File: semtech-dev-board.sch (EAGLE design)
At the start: 58 parts, among them Q1 BSS123, Q2 32MHz, U1 SEMTECH_SX1236, U3 MIC5219 3.3V, X1 BU-SMA-G, X2 BU-SMA-G, X3 BU-SMA-G, X4 BU-SMA-G

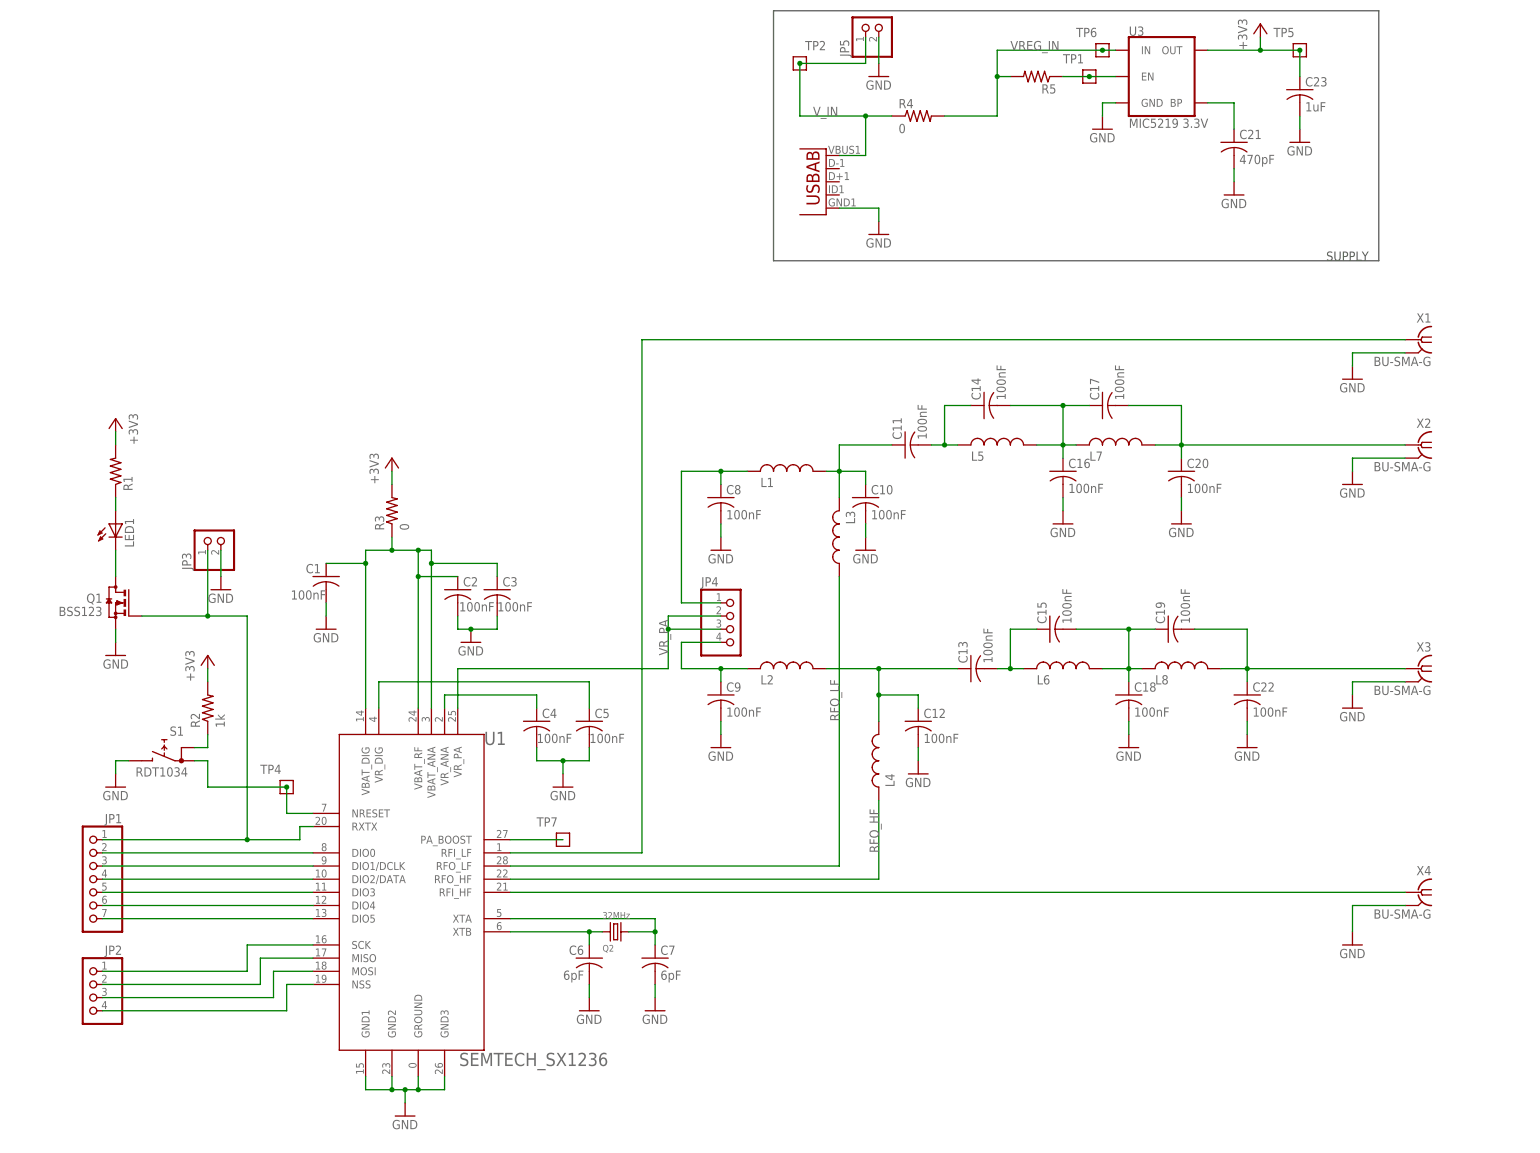
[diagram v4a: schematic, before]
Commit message: Removed caps
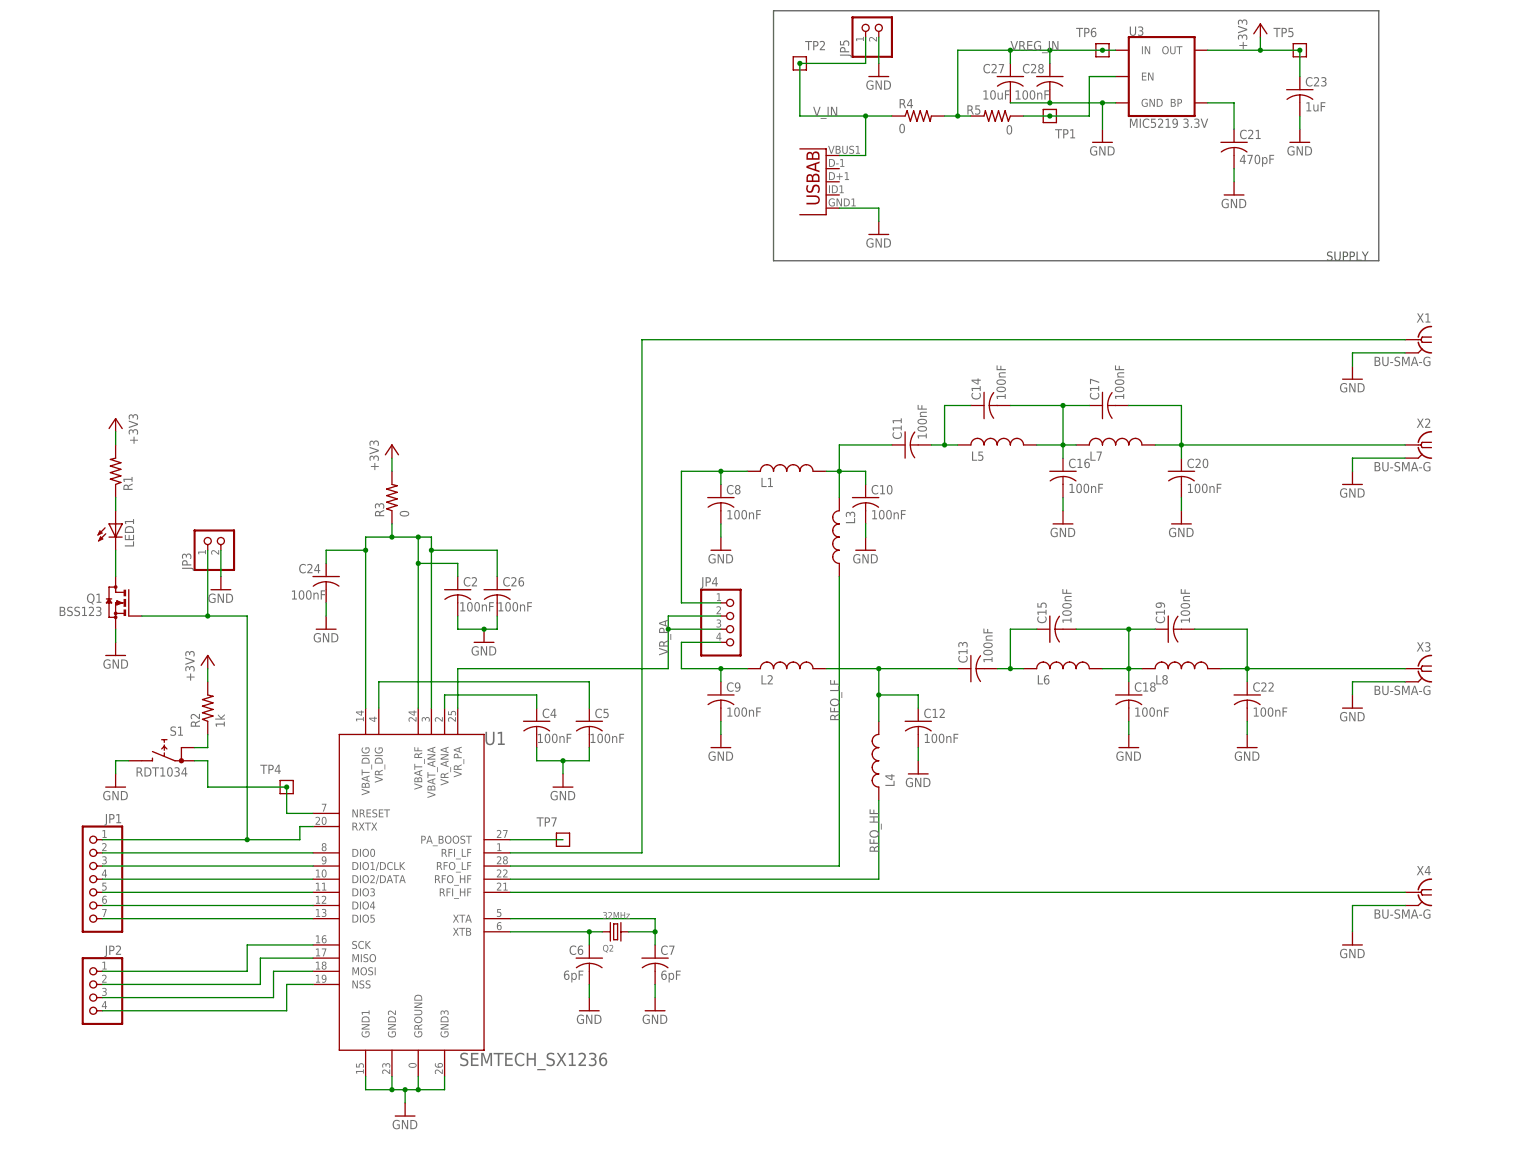
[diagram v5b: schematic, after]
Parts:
- added C27: 10uF, rcl:C-USC0805
- added C28: 100nF, rcl:C-USC0805
- R5: value (none) -> 0
- renumbered C1 to C24, C3 to C26
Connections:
- net 5219_EN renamed N$1
- net GND: now also C27.2, C28.2
- net VREG_IN: now also C27.1, C28.1
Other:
- moved on the sheet: R3, R5, TP1

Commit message: Components placed, 80% routed
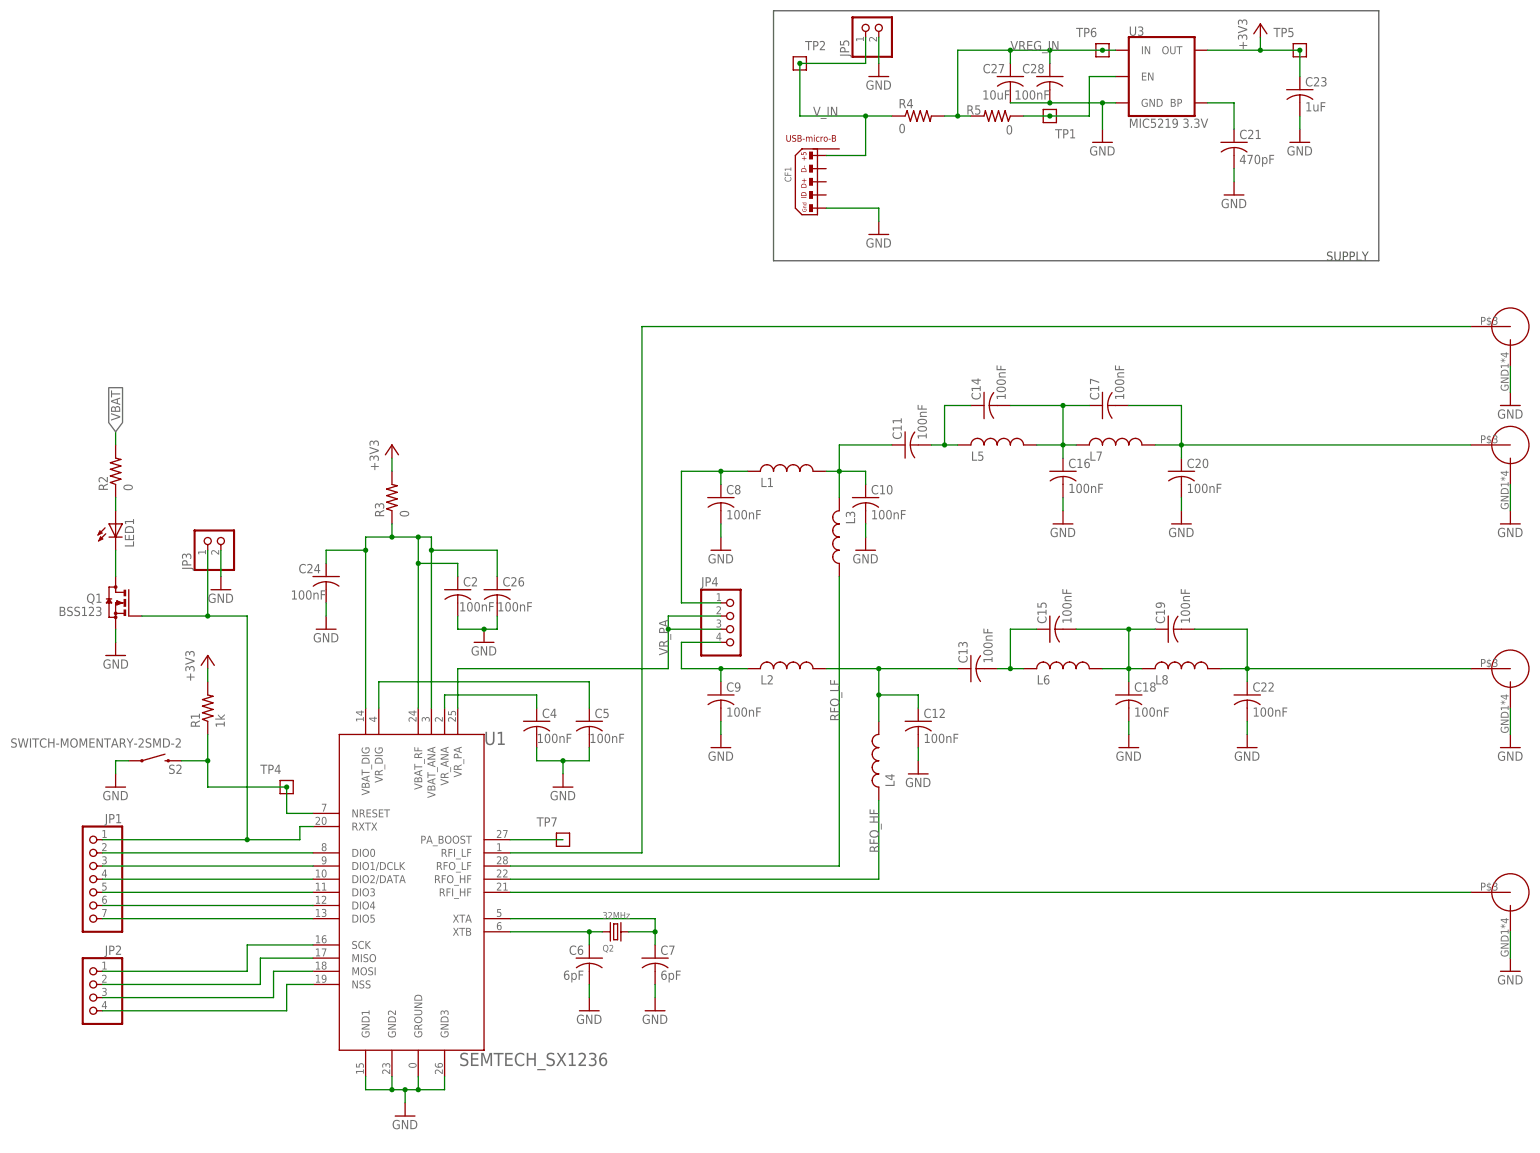
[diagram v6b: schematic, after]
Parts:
- removed S1: RDT1034, switch:RDT1034
- removed U2: (no value), microusb:USB""
- removed X1, X2, X3, X4: BU-SMA-G, con-coax:BU-SMA-G
- added CF1: (no value), psas_c3_team05:CON_USB-MICRO-B-RECEPTACLE-PTH-HIROSE-ZX62D-B-5P8
- added S2: SWITCH-MOMENTARY-2SMD-2, psas_c3_team05:SWITCH-MOMENTARY-2SMD-2
- added U$1, U$2, U$3, U$4: SMAJ716-ND, psas_c3_team05:SMAJ716-ND
- R1: value (none) -> 1k; device rcl:R-US_M0805 -> rcl:R-US_R0805
- R2: value 1k -> 0
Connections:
- removed net RST_SUP: R2.1, S1.A
- net +3V3: no longer R2.2
- net GND: now also CF1.5, S2.1, U$1.OUTERCONDUCTOR, U$2.OUTERCONDUCTOR, U$3.OUTERCONDUCTOR, U$4.OUTERCONDUCTOR; no longer S1.B, U2.GND, X1.2, X2.2, X3.2, X4.2
- net LED+: now also R2.1; no longer R1.1
- net RFI_HF: now also U$4.CENTERCONDUCTOR; no longer X4.1
- net RFI_LF: now also U$1.CENTERCONDUCTOR; no longer X1.1
- net RFO_HF_OUT: now also U$3.CENTERCONDUCTOR; no longer X3.1
- net RFO_LF_OUT: now also U$2.CENTERCONDUCTOR; no longer X2.1
- net SX1236_RST: now also R1.1, S2.2; no longer S1.A1
- net VBAT: now also R2.2
- net V_IN: now also CF1.1; no longer U2.VBUS
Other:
- moved on the sheet: R1, R2

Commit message: 97% routed, needs vias, mounts, scope clips, and vals
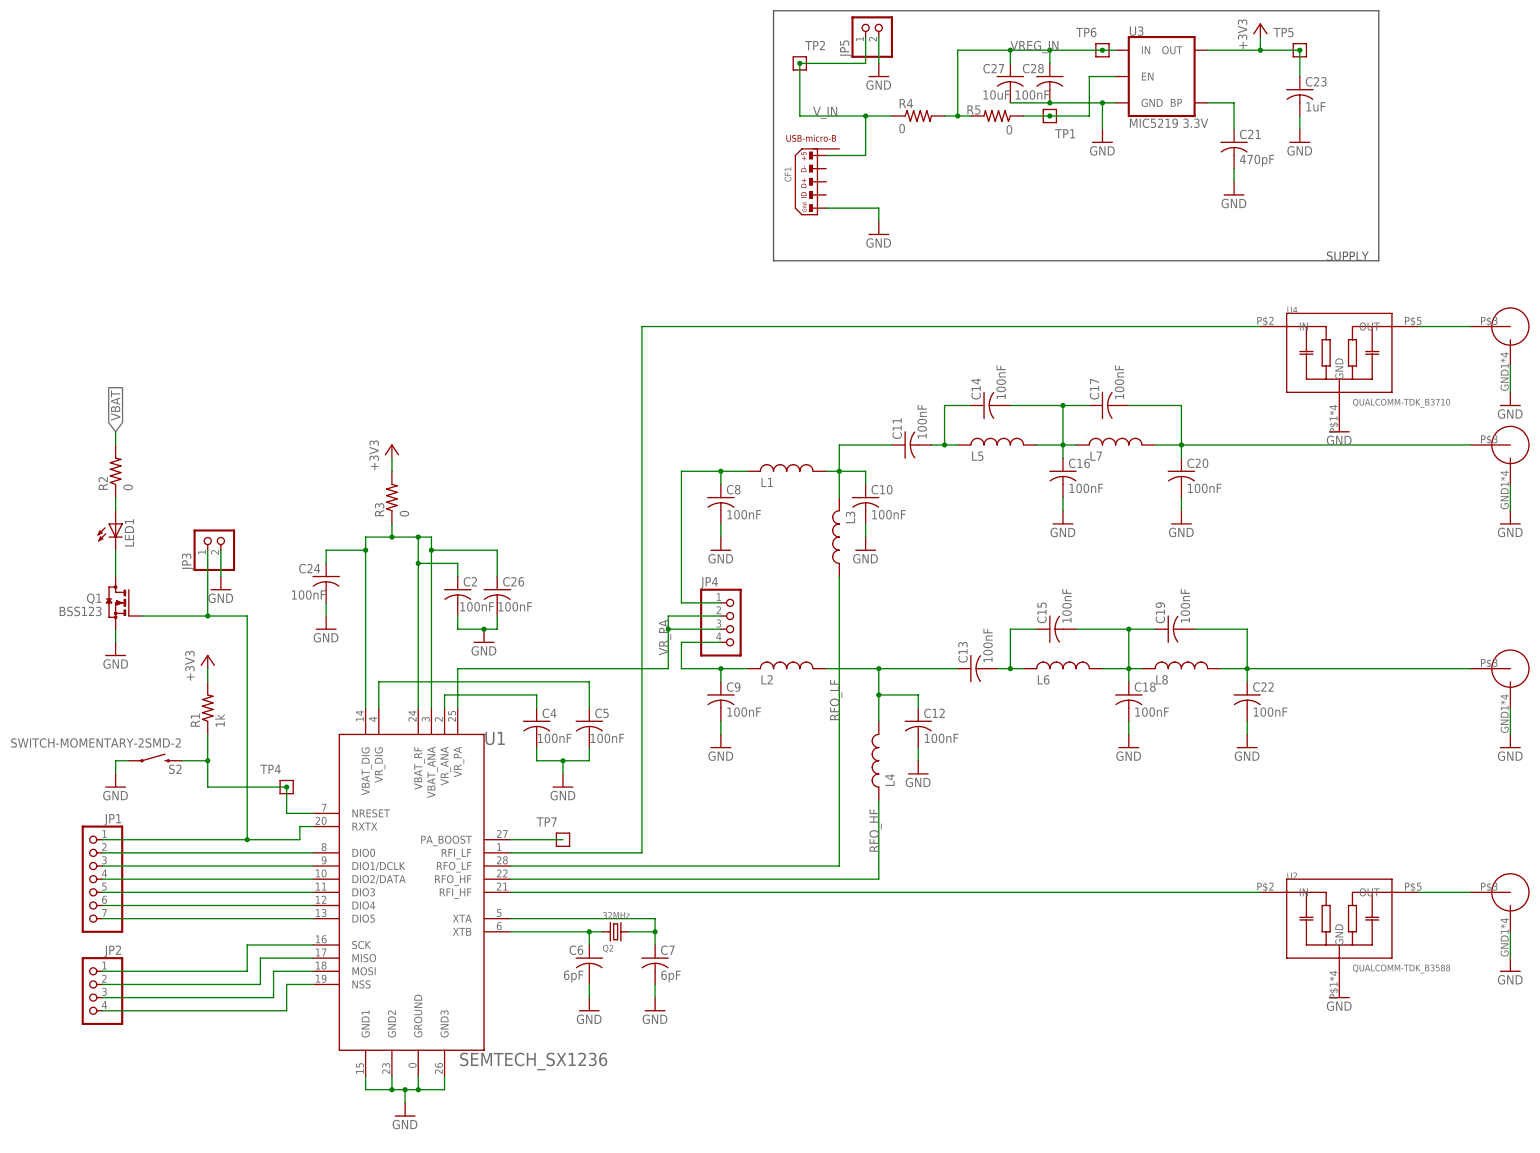
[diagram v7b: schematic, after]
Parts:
- added U2: QUALCOMM-TDK_B3588, low-gain-radio:QUALCOMM-TDK_B3588
- added U4: QUALCOMM-TDK_B3710, low-gain-radio:QUALCOMM-TDK_B3710
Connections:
- new net N$5: U$1.CENTERCONDUCTOR, U4.OUT
- new net RFI_HF_ANT: U$4.CENTERCONDUCTOR, U2.OUT
- net GND: now also U2.GND, U4.GND
- net RFI_HF: now also U2.IN; no longer U$4.CENTERCONDUCTOR
- net RFI_LF: now also U4.IN; no longer U$1.CENTERCONDUCTOR

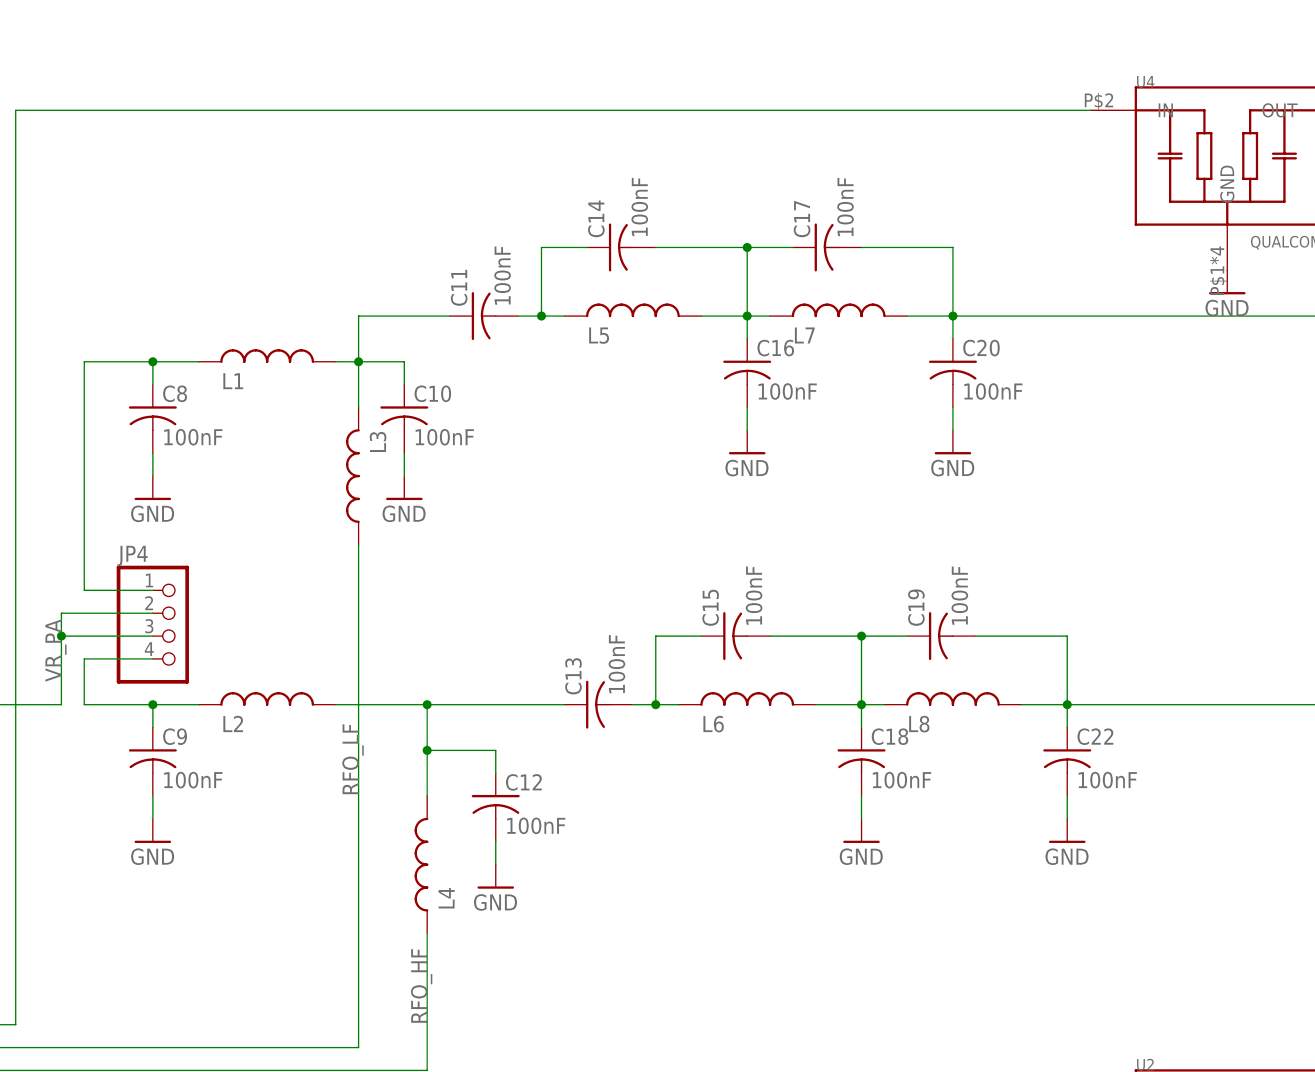
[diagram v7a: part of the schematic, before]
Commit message: Filter values updated
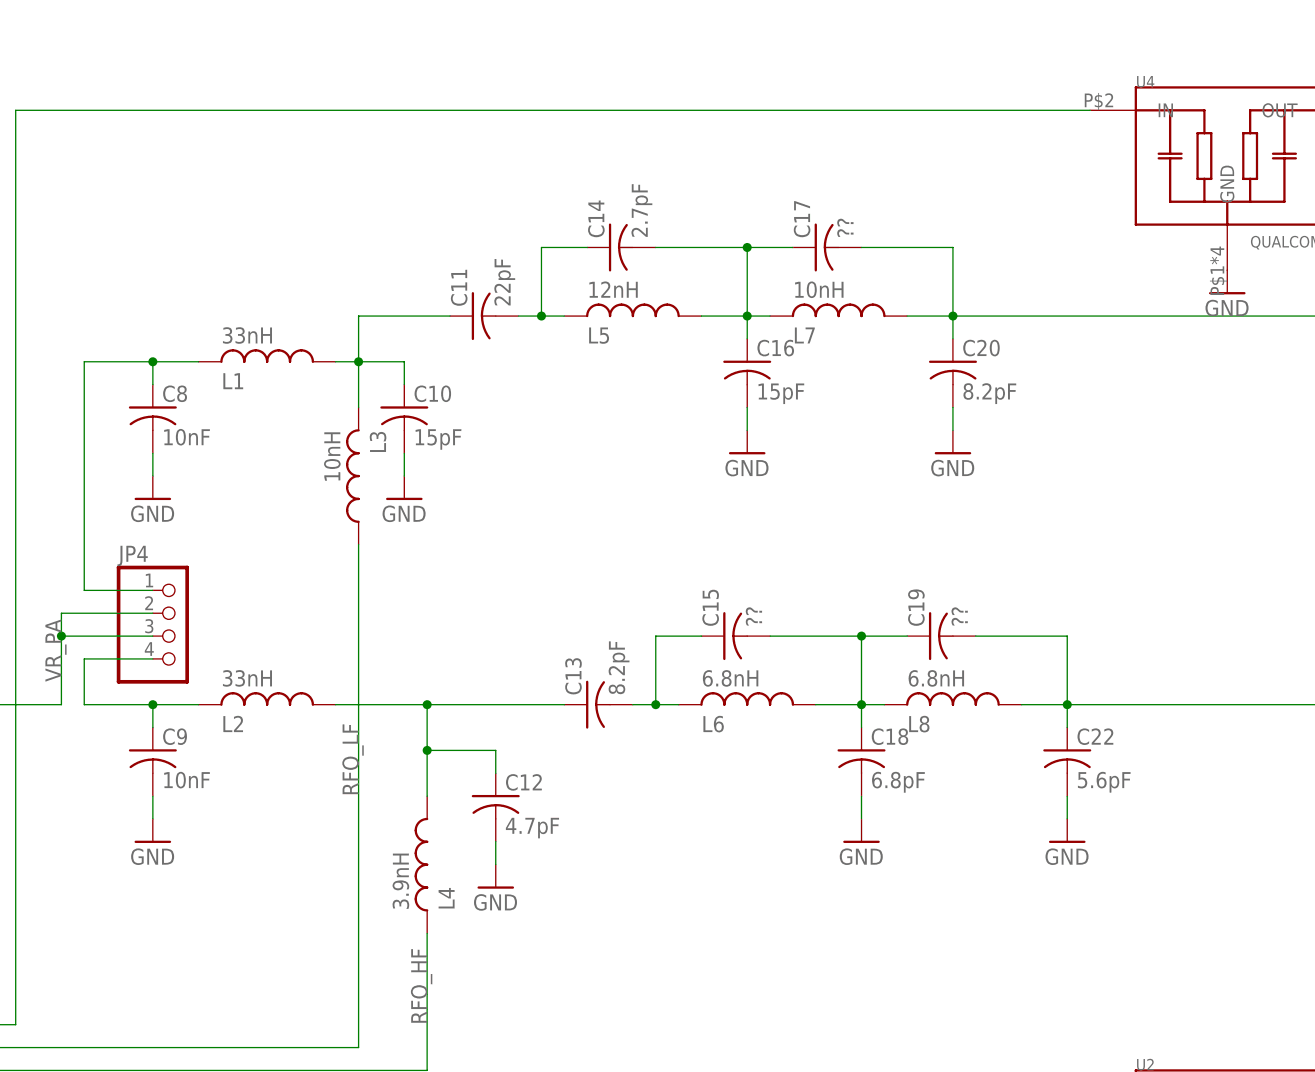
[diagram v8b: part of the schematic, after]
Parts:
- C10, C16: value 100nF -> 15pF
- C11: value 100nF -> 22pF
- C12: value 100nF -> 4.7pF
- C13, C20: value 100nF -> 8.2pF
- C14: value 100nF -> 2.7pF
- C15, C17, C19: value 100nF -> ??
- C18: value 100nF -> 6.8pF
- C22: value 100nF -> 5.6pF
- C8, C9: value 100nF -> 10nF
- L1, L2: value (none) -> 33nH
- L3, L7: value (none) -> 10nH
- L4: value (none) -> 3.9nH
- L5: value (none) -> 12nH
- L6, L8: value (none) -> 6.8nH
